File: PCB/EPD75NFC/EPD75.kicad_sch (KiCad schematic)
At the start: 168 parts, among them J1 Conn_01x26, J10 TF_PUSH, J11 Reset, J12 TC2030-USB-NL-DS, J2 PWR, J3 NFC, J4 BTN, J5 USB-C-Socket-H, J7 USB-C-Socket-H, J8 PWR, Q1 BSS138, SW2 ESE13V01D, T1 T3902_MEMS_Mic, U1 TPS562246, U2 PN532, U3 SCD41, U4 ESP32-S3-MINI-1, U5 GZP6816D, U7 SHT40, Y1 27.12MHz

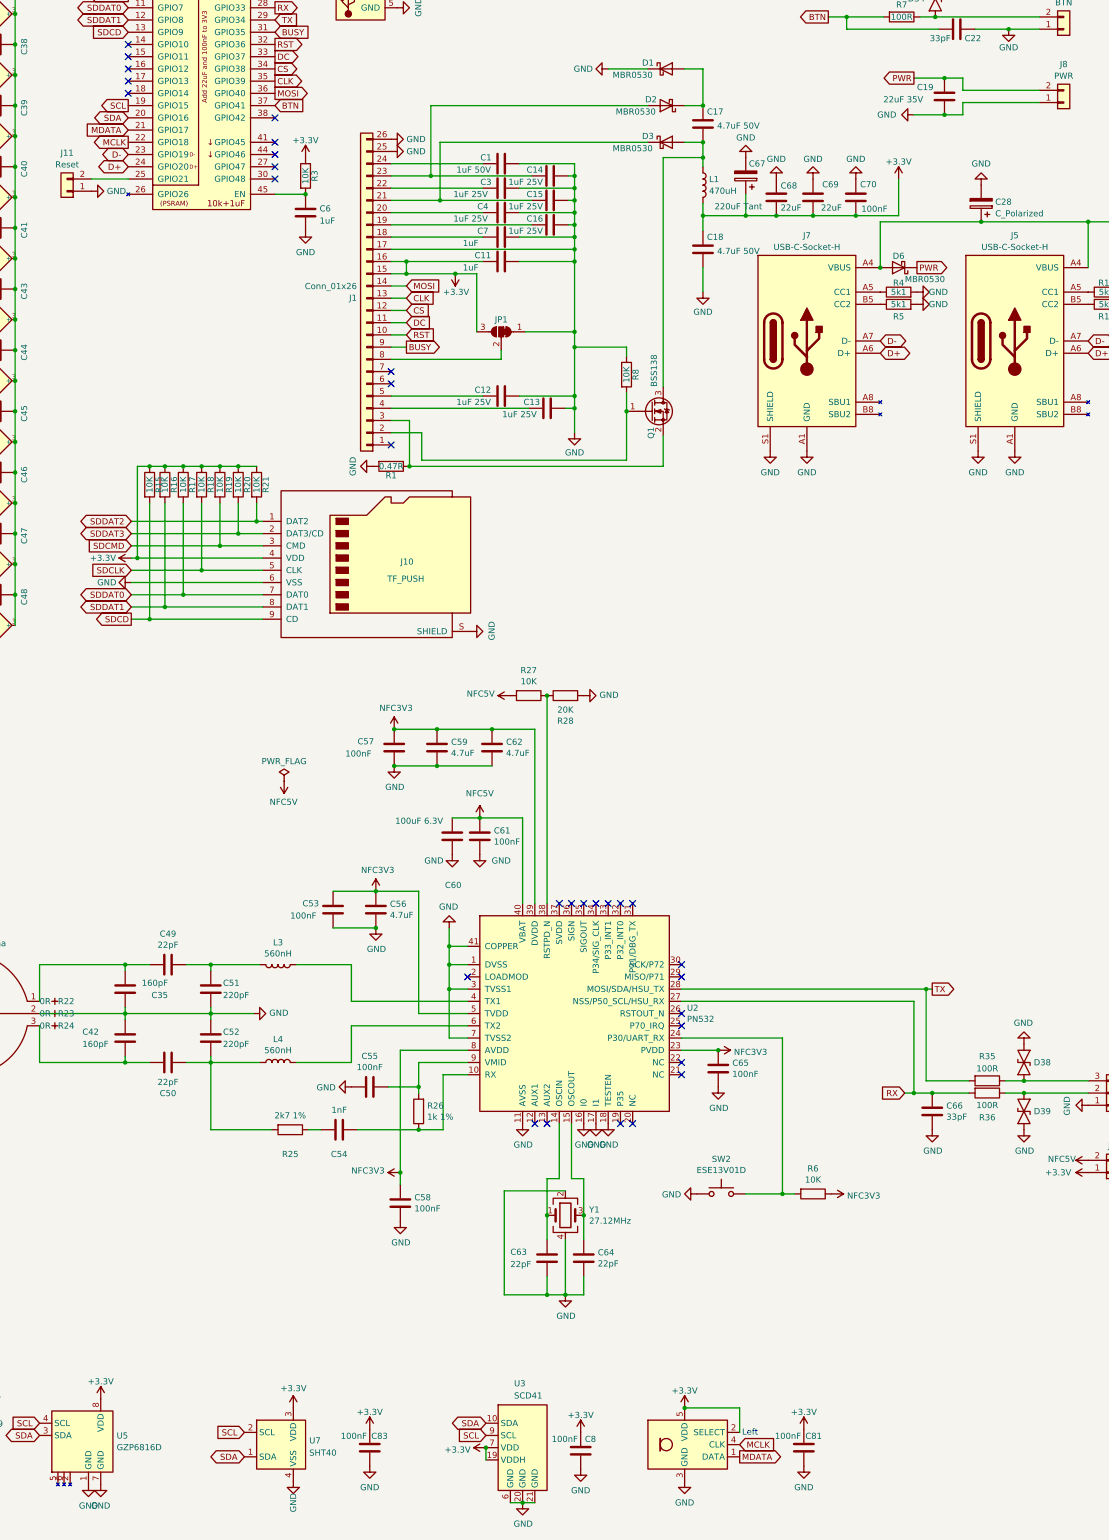
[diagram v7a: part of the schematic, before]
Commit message: ADded DS18B20
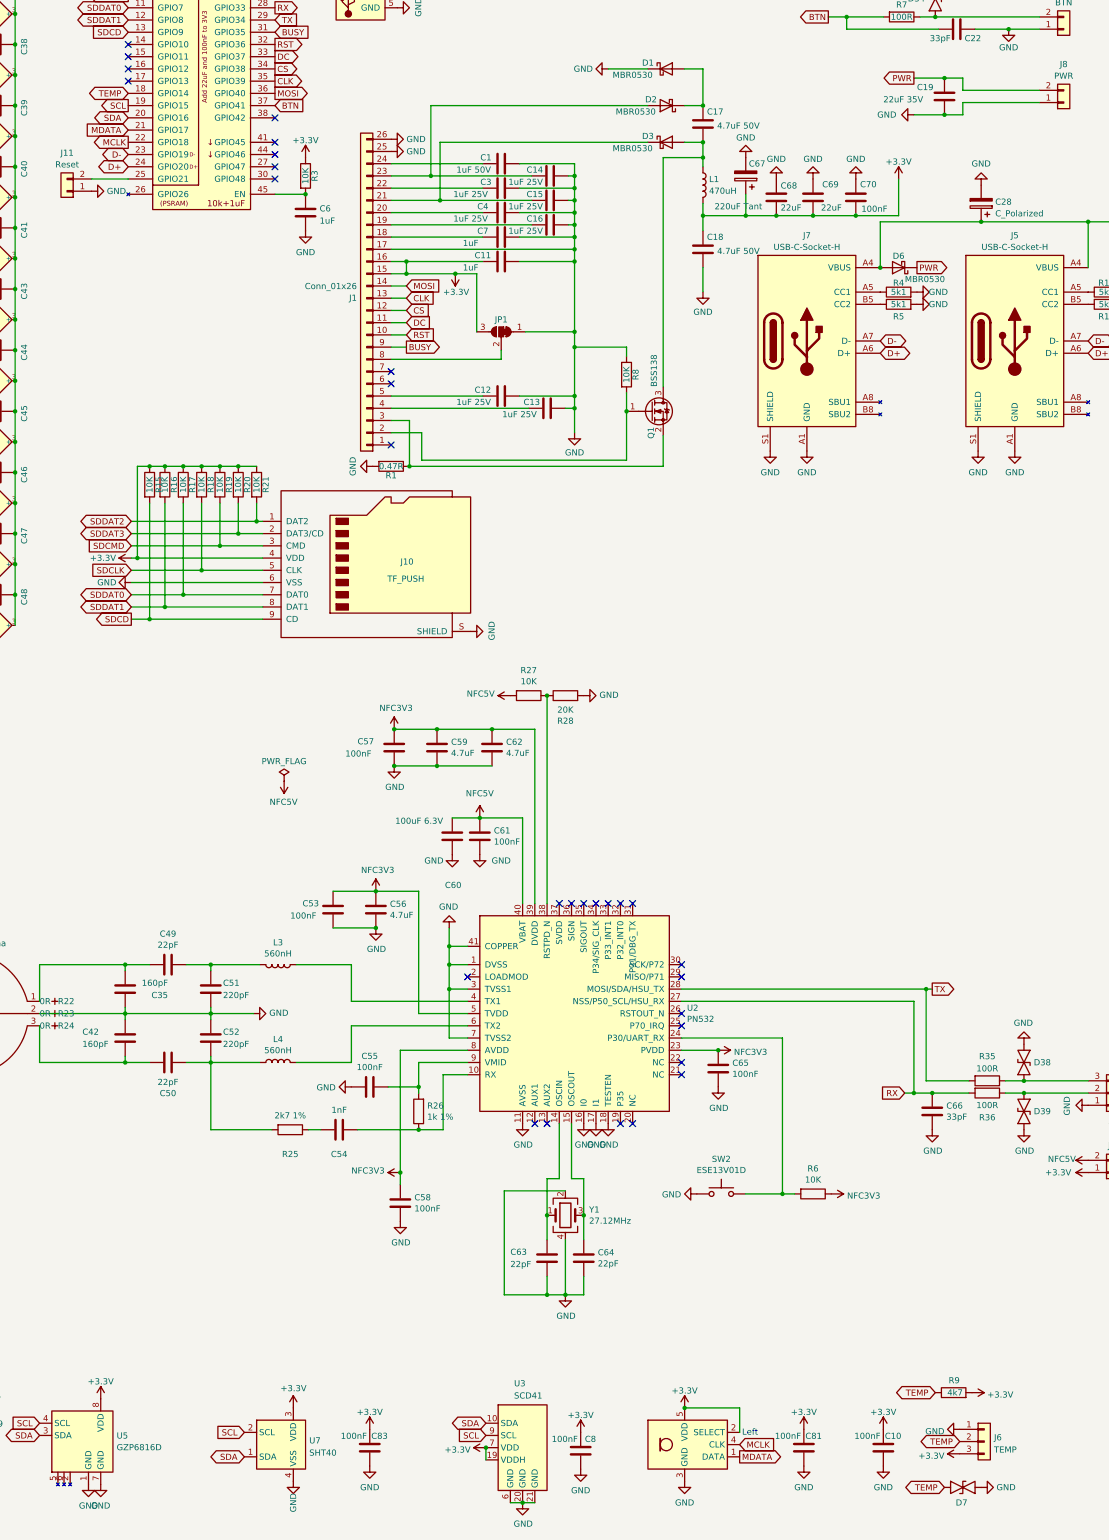
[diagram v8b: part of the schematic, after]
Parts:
- added C10: 100nF, RevK:C_0201, symbol Device:C
- added D7: ~, RevK:DFN1006-2L, symbol RevK:ES05D1MC10
- added J6: TEMP, RevK:WAGO-2060-453-998-404, symbol Connector_Generic:Conn_01x03
- added R9: 4k7, RevK:R_0201, symbol Device:R
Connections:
- net +3.3V: now also C10.2, J6.3 (Pin_3), R9.2
- net GND: now also C10.1, D7.1, J6.1 (Pin_1)
- net TEMP: now reaches U4.18 (GPIO14)
- net TEMP: now also D7.2, J6.2 (Pin_2), R9.1
- no-connect marks 36 -> 35
